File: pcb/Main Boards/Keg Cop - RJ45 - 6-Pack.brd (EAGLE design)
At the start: 29.9 x 43.2 mm, 3 parts, among them X1 RJ45-8X, X2 RJ45-8X

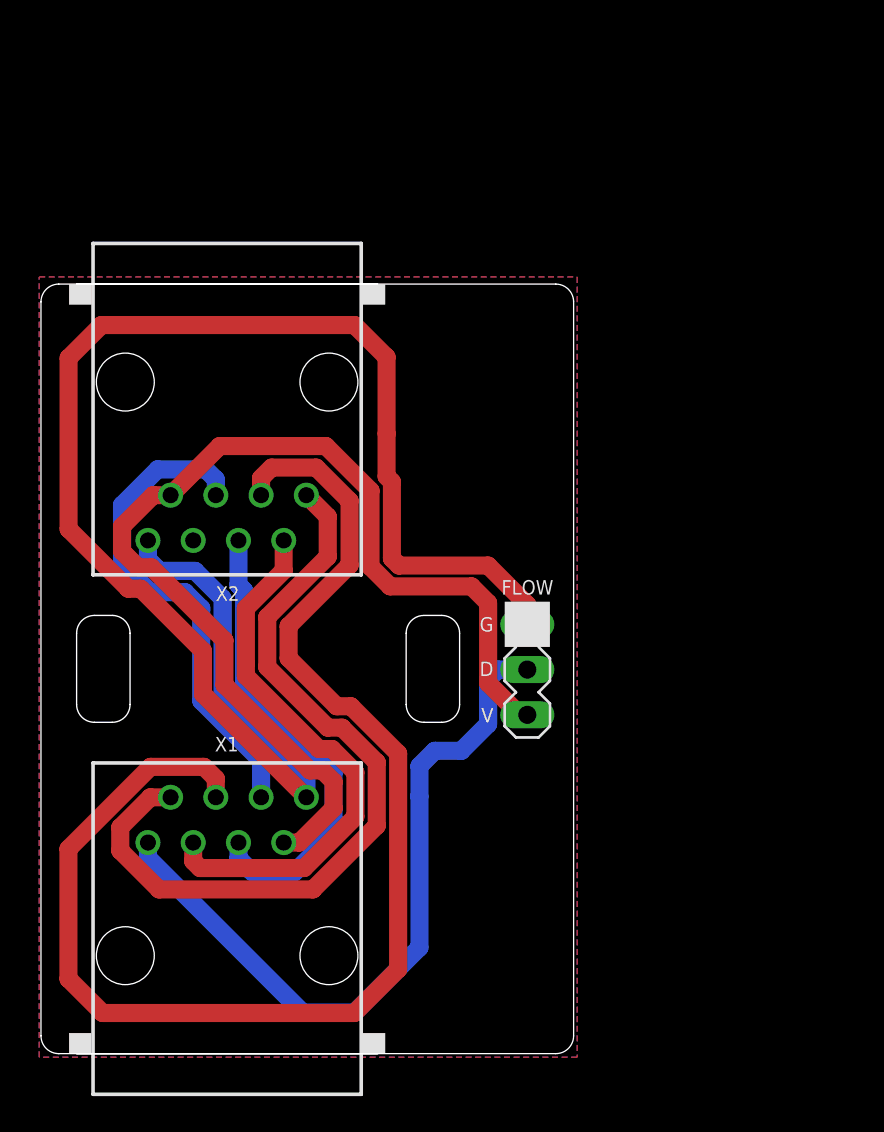
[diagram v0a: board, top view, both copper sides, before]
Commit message: Swap pins, split dirs
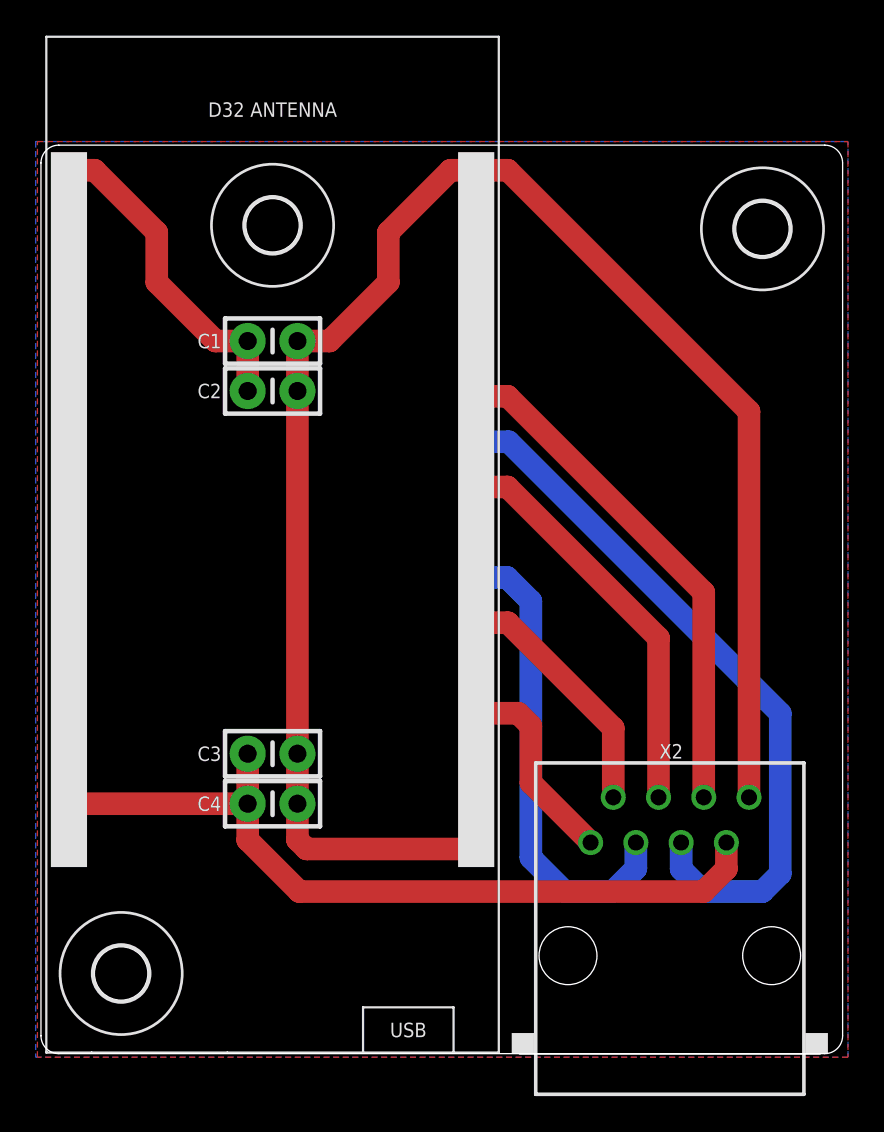
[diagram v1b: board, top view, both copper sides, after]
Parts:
- removed FLOW: (no value), Donnie:HDR-3_VERT
- removed X1: RJ45-8X, con-tycoelectronics:RJ45-NO-SHIELD
- added C1, C3: 0.1μF, Donnie:CAP_PTH-2.54
- added C2, C4: 1.0μF, Donnie:CAP_PTH-2.54
- added D32: Lolin D32, Donnie:D32_NO_BATT
- added U$1, U$2, U$3: (no value), holes:3,0
- moved X2 40.7 mm to (35.3, 5.50), turned to 0 degrees
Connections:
- removed net FLOW: FLOW.2, X1.1
- removed net N$1: X1.2, X2.1
- removed net N$2: X1.3, X2.2
- removed net N$3: X1.4, X2.3
- removed net N$5: X1.5, X2.4
- removed net N$7: X1.6, X2.5
- new net KEG1: D32.IO0, X2.1
- new net KEG2: D32.IO16, X2.2
- new net KEG3: D32.IO17, X2.3
- new net KEG4: D32.IO18, X2.4
- new net KEG5: D32.IO19, X2.5
- new net KEG6: D32.IO21, X2.6
- new net VCC: C1.1, C2.1, D32.VCC
- net 5V: now also C3.1, C4.1, D32.VBUS; no longer FLOW.3, X1.7
- net GND: now also C1.2, C2.2, C3.2, C4.2, D32.GND, D32.GND2; no longer FLOW.1, X1.8
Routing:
- net N$3: track 76.8 -> 0.00 mm
- net N$1: track 45.1 -> 0.00 mm
- net FLOW: track 41.2 -> 0.00 mm
- net KEG5: track 0.00 -> 40.4 mm
- net N$2: track 30.9 -> 0.00 mm
- net KEG6: track 0.00 -> 28.8 mm
- net N$7: track 28.0 -> 0.00 mm
- net KEG3: track 0.00 -> 26.7 mm
- net N$5: track 26.1 -> 0.00 mm
- net KEG4: track 0.00 -> 22.7 mm
- net VCC: track 0.00 -> 18.4 mm
- net 5V: track 61.2 -> 44.9 mm
- net KEG2: track 0.00 -> 14.0 mm
- net KEG1: track 0.00 -> 11.3 mm
- net GND: track 90.4 -> 96.5 mm
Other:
- board size 29.9 x 43.2 mm -> 45 x 51 mm
- board text added: "1 - KEG1 2 - KEG2 3 - KEG3 4 - KEG4"
- board text added: "5 - KEG5 6 - KEG6 7 - KEG7 8 - KEG8"
- board text removed: "D"
- board text removed: "G"
- board text removed: "V"

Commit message: Renamed files
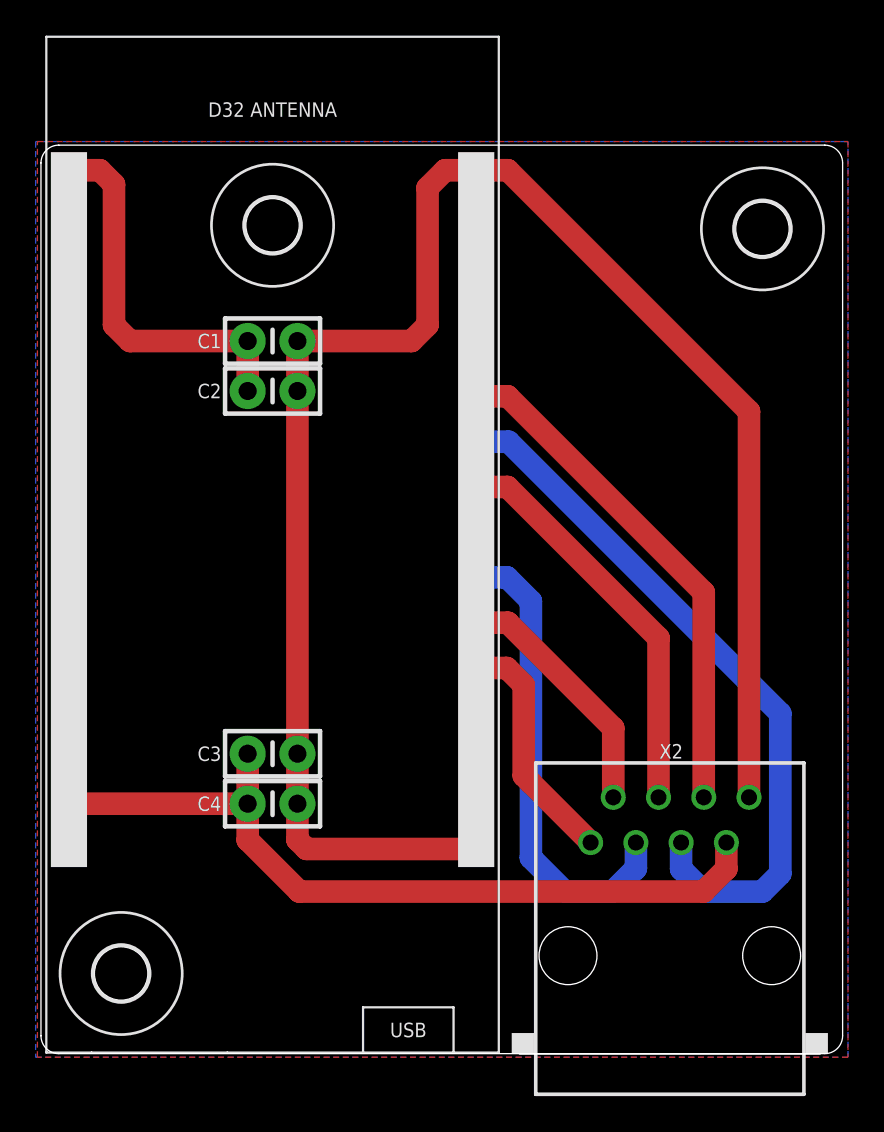
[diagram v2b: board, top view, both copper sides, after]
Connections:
- net KEG1: now also D32.IO4; no longer D32.IO0
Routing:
- net VCC: track 18.4 -> 21.4 mm
- net GND: track 96.5 -> 99.3 mm
- net KEG1: track 11.3 -> 13.5 mm
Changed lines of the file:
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@@
 <layer number="14" name="Route14" color="22" fill="1" visible="no" active="no"/>
 <layer number="15" name="Route15" color="23" fill="1" visible="no" active="no"/>
-<layer number="16" name="Bottom" color="1" fill="1" visible="yes" active="yes"/>
+<layer number="16" name="Bottom" color="1" fill="1" visible="no" active="yes"/>
 <layer number="17" name="Pads" color="2" fill="1" visible="yes" active="yes"/>
 <layer number="18" name="Vias" color="2" fill="1" visible="yes" active="yes"/>
@@
 <wire x1="14.397" y1="37.198" x2="14.397" y2="40.002" width="1.27" layer="1"/>
 <wire x1="14.397" y1="16.836" x2="14.397" y2="37.198" width="1.27" layer="1"/>
-<wire x1="14.397" y1="40.002" x2="16.202" y2="40.002" width="1.27" layer="1"/>
-<wire x1="19.5" y1="43.3" x2="19.5" y2="46.1" width="1.27" layer="1"/>
-<wire x1="19.5" y1="46.1" x2="22.99" y2="49.59" width="1.27" layer="1"/>
-<wire x1="22.99" y1="49.59" x2="24.43" y2="49.59" width="1.27" layer="1"/>
-<wire x1="16.202" y1="40.002" x2="19.5" y2="43.3" width="1.27" layer="1"/>
+<wire x1="14.397" y1="40.002" x2="20.802" y2="40.002" width="1.27" layer="1"/>
+<wire x1="21.7" y1="40.9" x2="21.7" y2="48.6" width="1.27" layer="1"/>
+<wire x1="21.7" y1="48.6" x2="22.69" y2="49.59" width="1.27" layer="1"/>
+<wire x1="22.69" y1="49.59" x2="24.43" y2="49.59" width="1.27" layer="1"/>
+<wire x1="20.802" y1="40.002" x2="21.7" y2="40.9" width="1.27" layer="1"/>
 <wire x1="39.745" y1="14.39" x2="39.745" y2="36.055" width="1.27" layer="1"/>
 <wire x1="26.21" y1="49.59" x2="24.43" y2="49.59" width="1.27" layer="1"/>
@@
 <signal name="KEG1">
 <contactref element="X2" pad="1"/>
-<contactref element="D32" pad="IO0"/>
-<wire x1="27.5" y1="18.4" x2="27.5" y2="15.205" width="1.27" layer="1"/>
-<wire x1="27.5" y1="18.4" x2="26.79" y2="19.11" width="1.27" layer="1"/>
-<wire x1="26.79" y1="19.11" x2="24.43" y2="19.11" width="1.27" layer="1"/>
-<wire x1="27.5" y1="15.205" x2="30.855" y2="11.85" width="1.27" layer="1"/>
+<wire x1="30.855" y1="11.85" x2="27.5" y2="15.205" width="1.27" layer="1"/>
+<contactref element="D32" pad="IO4"/>
+<wire x1="27.5" y1="15.205" x2="27.1" y2="15.605" width="1.27" layer="1"/>
+<wire x1="27.1" y1="15.605" x2="27.1" y2="20.7" width="1.27" layer="1"/>
+<wire x1="27.1" y1="20.7" x2="26.15" y2="21.65" width="1.27" layer="1"/>
+<wire x1="26.15" y1="21.65" x2="24.43" y2="21.65" width="1.27" layer="1"/>
 </signal>
 <signal name="KEG2">
@@
 <contactref element="C2" pad="1"/>
 <wire x1="11.603" y1="37.198" x2="11.603" y2="40.002" width="1.27" layer="1"/>
-<wire x1="1.57" y1="49.59" x2="3.01" y2="49.59" width="1.27" layer="1"/>
-<wire x1="6.5" y1="46.1" x2="6.5" y2="43.3" width="1.27" layer="1"/>
-<wire x1="9.798" y1="40.002" x2="11.603" y2="40.002" width="1.27" layer="1"/>
-<wire x1="3.01" y1="49.59" x2="6.5" y2="46.1" width="1.27" layer="1"/>
-<wire x1="6.5" y1="43.3" x2="9.798" y2="40.002" width="1.27" layer="1"/>
+<wire x1="1.57" y1="49.59" x2="3.31" y2="49.59" width="1.27" layer="1"/>
+<wire x1="4.1" y1="48.8" x2="4.1" y2="40.9" width="1.27" layer="1"/>
+<wire x1="4.998" y1="40.002" x2="11.603" y2="40.002" width="1.27" layer="1"/>
+<wire x1="3.31" y1="49.59" x2="4.1" y2="48.8" width="1.27" layer="1"/>
+<wire x1="4.1" y1="40.9" x2="4.998" y2="40.002" width="1.27" layer="1"/>
 </signal>
 </signals>
